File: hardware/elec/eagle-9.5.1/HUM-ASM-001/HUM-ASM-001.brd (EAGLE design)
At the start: 99.1 x 99.1 mm, 63 parts, among them J2 75869-131LF, J20 75869-131LF, J21 75869-131LF, J3 B2B-XH-AM(LF)(SN), K1 7-1393239-7, K2 7-1393239-7, Q1 IRLB8721PBF, Q2 IRLB8721PBF, U1 MCP23017-E/SP

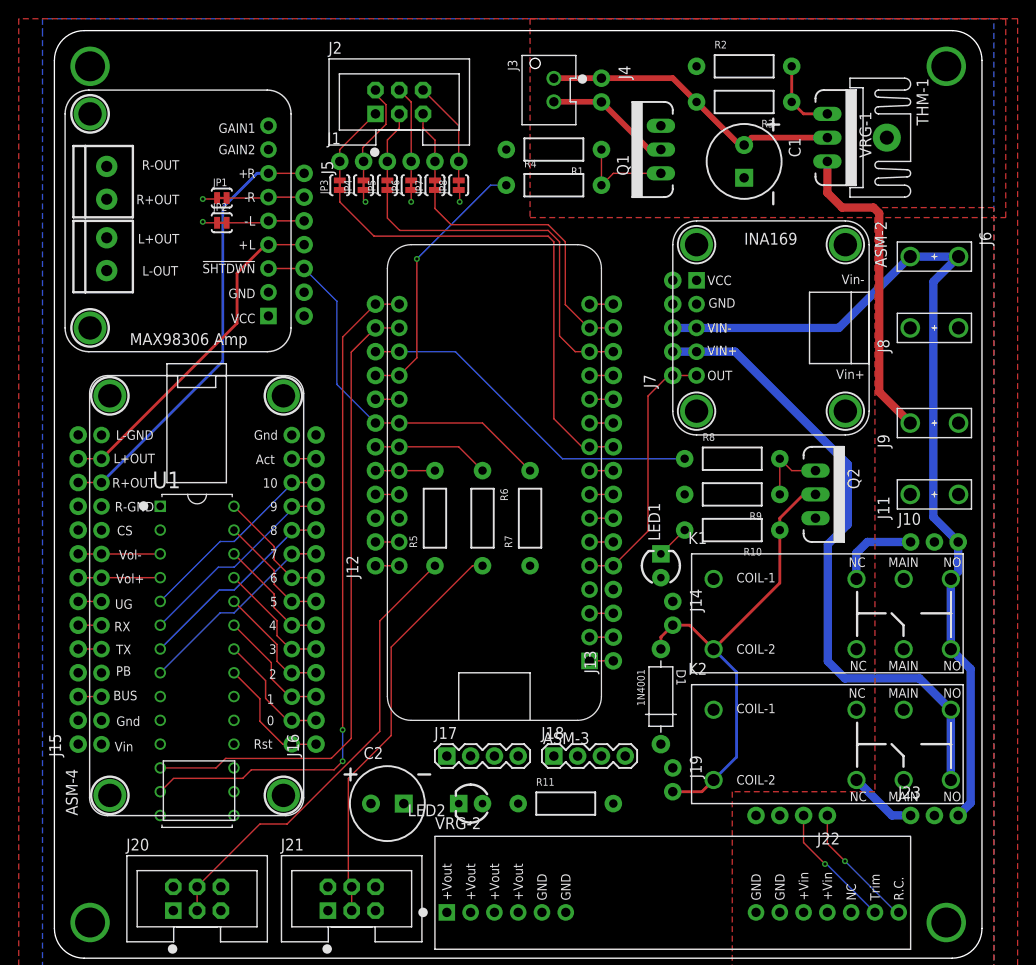
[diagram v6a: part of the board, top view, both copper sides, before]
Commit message: * PCB Silk cleanup completed
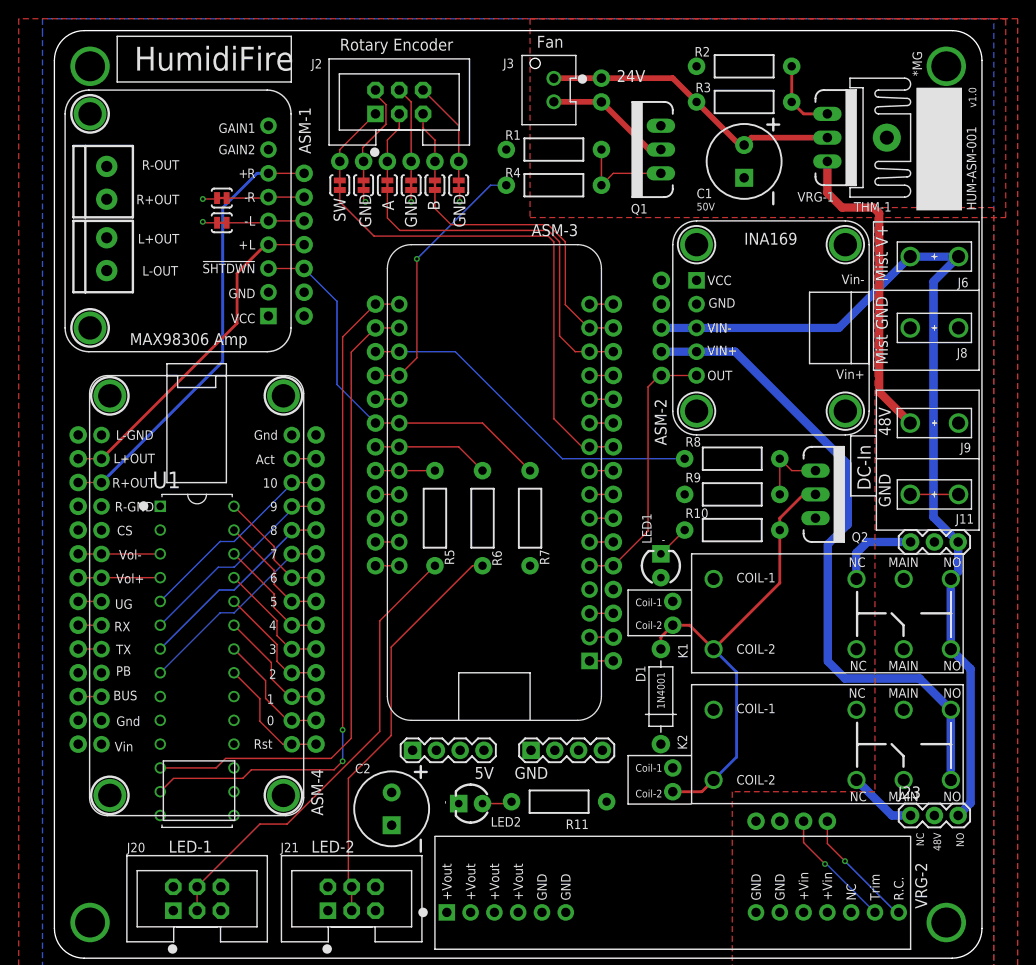
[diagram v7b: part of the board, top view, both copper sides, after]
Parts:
- J10, J23: device MG-Eagle_v1:1X03_NO_SILK -> MG-Eagle_v1:1X03
- moved J17 3.71 mm to (38.3, 22.2)
- moved J18 2.51 mm to (50.9, 22.2)
- moved J7 1.22 mm to (64.8, 62.2)
- moved R11 0.74 mm to (53.9, 16.7), turned to 180 degrees
- moved C2 0.72 mm to (36.0, 16.0), turned to 270 degrees
- moved J22 0.61 mm to (82.5, 14.6)
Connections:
- net 5V: now also R11.P$1; no longer LED2.K
- net GND: now also LED2.K; no longer R11.P$2
- net N$19: now also R11.P$2; no longer R11.P$1
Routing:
- net GND: track 7.07 -> 12.2 mm
- net N$19: track 0.00 -> 3.18 mm
- net N$16: track 68.4 -> 69.6 mm
- net MIST-VIN: track 97.3 -> 98.5 mm
- net SFX-ROUT: track 48.0 -> 47.4 mm
- net N$29: track 13.6 -> 13.0 mm
- net N$27: track 13.7 -> 13.1 mm
- net CRNT-MON: track 28.3 -> 28.9 mm
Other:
- board text added: "*MG"
- board text added: "-"
- board text added: "24V"
- board text added: "48V"
- board text added: "50V"
- board text added: "5V"
- board text added: "A"
- board text added: "B"
- board text added: "Coil-1"
- board text added: "Coil-2"
- board text added: "DC-In"
- board text added: "Fan"
- board text added: "GND"
- board text added: "HUM-ASM-001"
- board text added: "HumidiFire"
- board text added: "LED-1"
- board text added: "LED-2"
- board text added: "Mist GND"
- board text added: "Mist V+"
- board text added: "NC"
- board text added: "NO"
- board text added: "Rotary Encoder"
- board text added: "SW"
- board text added: "v1.0"

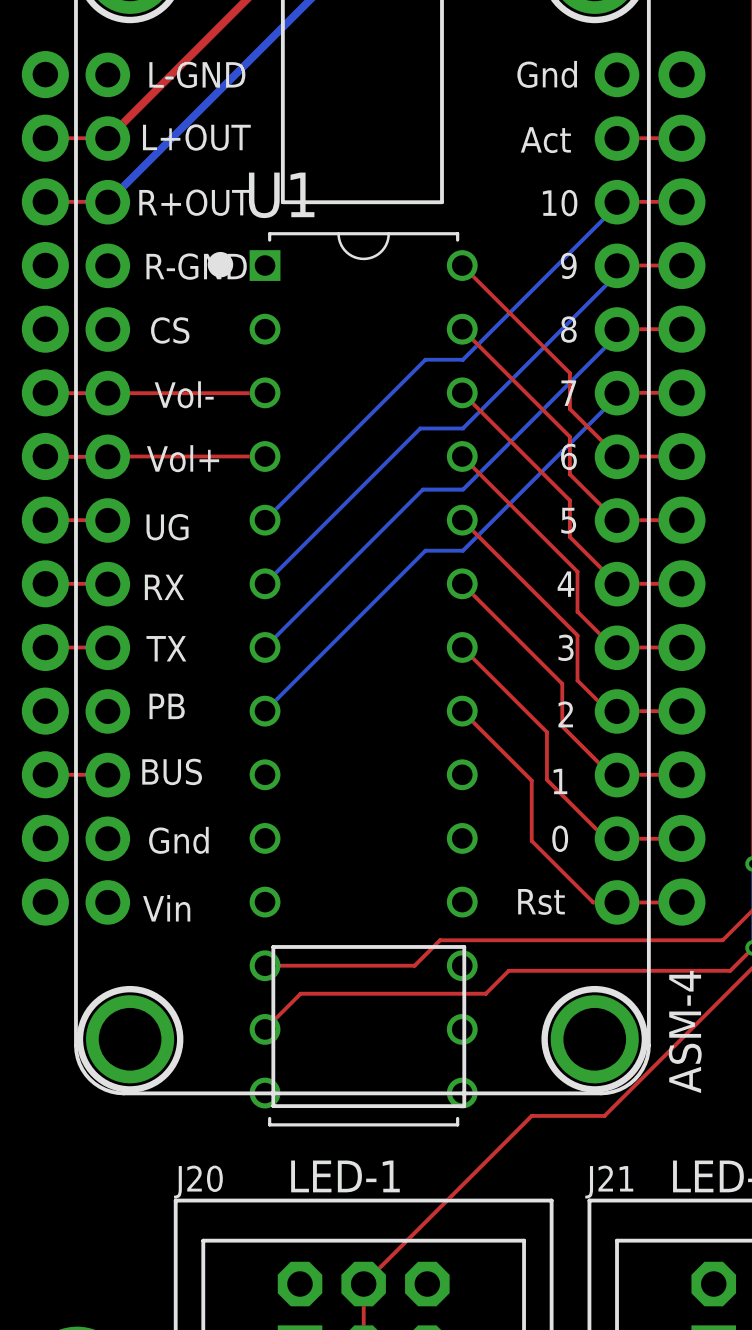
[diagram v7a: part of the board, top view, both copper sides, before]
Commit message: * Final PCB v1.0 edits * Exported Gerber files and send to fab
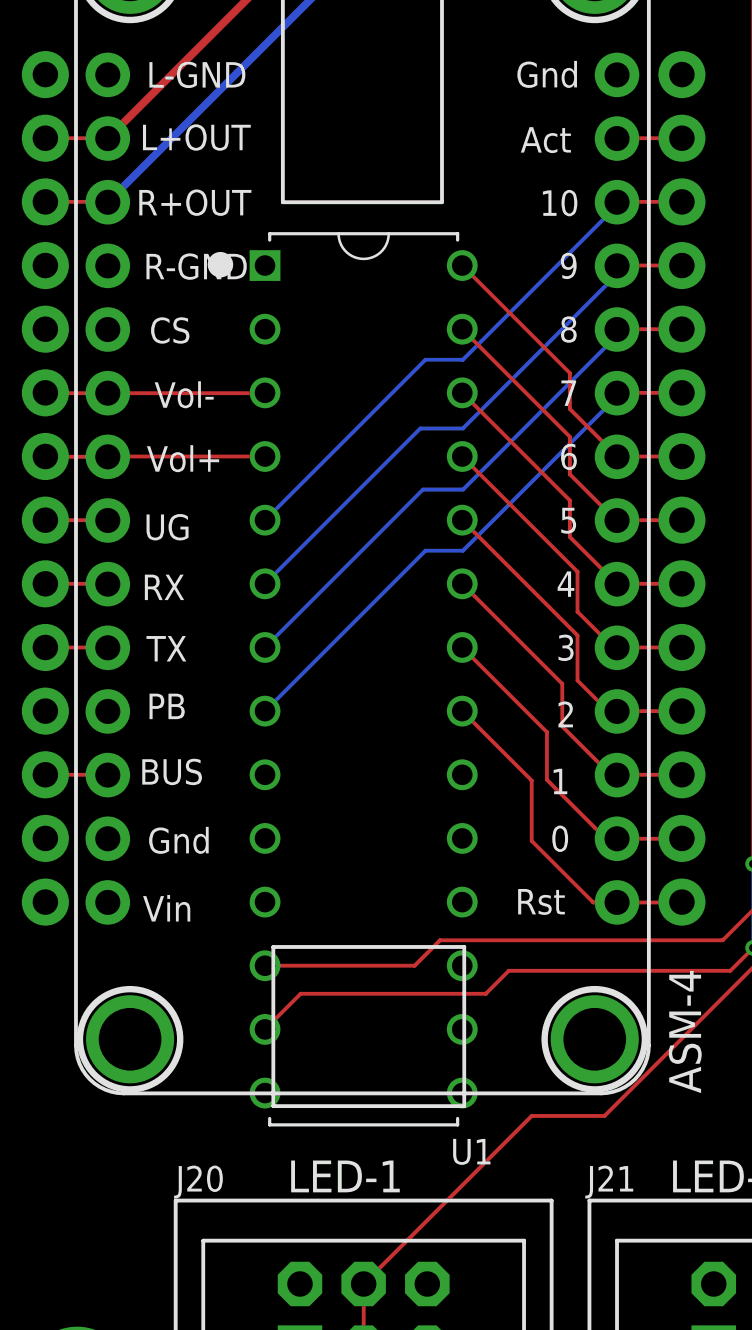
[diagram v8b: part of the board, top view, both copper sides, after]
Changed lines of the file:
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@@
 <attribute name="MF" value="Microchip" x="67.31" y="10.16" size="1.778" layer="27" display="off"/>
 <attribute name="MP" value="MCP23017-E/SP" x="67.31" y="10.16" size="1.778" layer="27" display="off"/>
-<attribute name="NAME" x="10.47133125" y="50.1886" size="1.781040625" layer="25"/>
+<attribute name="NAME" x="18.70093125" y="12.3934" size="1.016" layer="25"/>
 <attribute name="PACKAGE" value="DIP-28 Microchip" x="67.31" y="10.16" size="1.778" layer="27" display="off"/>
 </element>
